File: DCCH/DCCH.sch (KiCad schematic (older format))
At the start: 37 parts, among them J1 Conn_01x02, J2 Conn_01x02, J3 Conn_01x05, J4 Conn_01x05, J5 Conn_02x08_Odd_Even, U11 SN74HC595, U12 SN74HC595, U13 SN74HC595, U14 SN74HC595, U21 SN754410, U22 SN754410, U23 SN754410, U24 SN754410

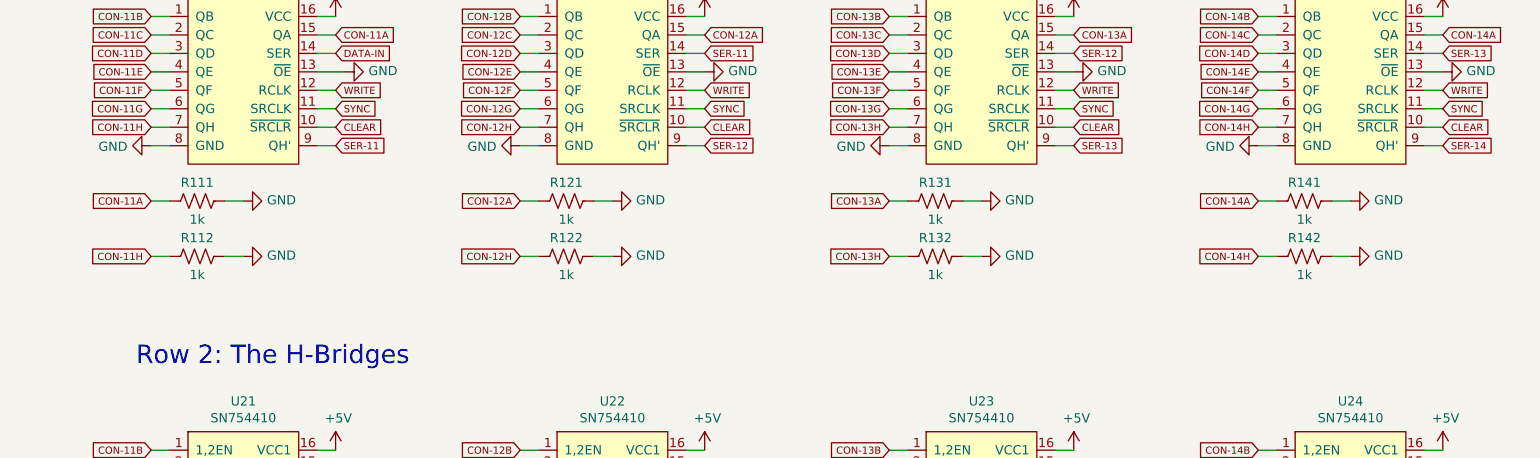
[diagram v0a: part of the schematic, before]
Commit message: Rewired everything. Removed the resistors. Now the control bit pattern for the shift registers makes sense.
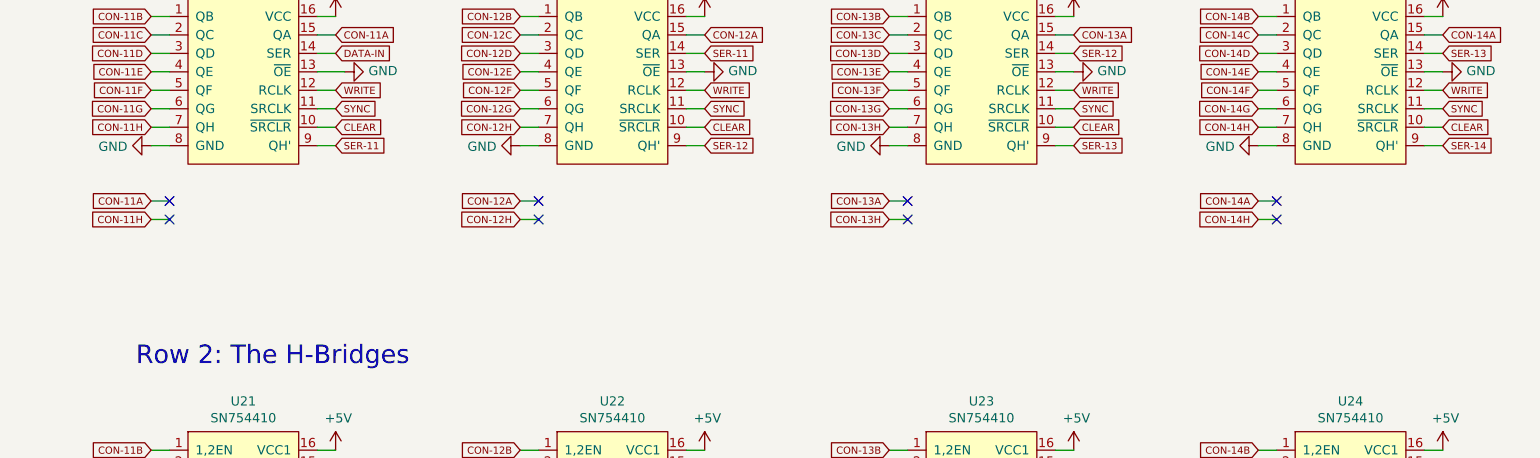
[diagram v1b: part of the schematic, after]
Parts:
- removed R111, R112, R121, R122, R131, R132, R141, R142: 1k, Resistor_THT:R_Axial_DIN0204_L3.6mm_D1.6mm_P5.08mm_Horizontal, symbol Device:R_US
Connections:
- no-connect marks 0 -> 8
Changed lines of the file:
@@
 Text GLabel 3300 2600 0    39   Input ~ 0
 CON-12A
-Text GLabel 3300 2900 0    39   Input ~ 0
+Text GLabel 3300 2700 0    39   Input ~ 0
 CON-12H
-$Comp
-L power:GND #PWR0151
-U 1 1 5F1FD99A
-P 3800 2600
-F 0 "#PWR0151" H 3800 2350 50  0001 C CNN
-F 1 "GND" V 3805 2472 50  0000 R CNN
-F 2 "" H 3800 2600 50  0001 C CNN
-F 3 "" H 3800 2600 50  0001 C CNN
-	1    3800 2600
-	0    -1   -1   0
-$EndComp
-Wire Wire Line
-	3700 2600 3800 2600
 Wire Wire Line
 	3300 2600 3400 2600
-$Comp
-L power:GND #PWR0150
-U 1 1 5F5CB761
-P 3800 2900
-F 0 "#PWR0150" H 3800 2650 50  0001 C CNN
-F 1 "GND" V 3805 2772 50  0000 R CNN
-F 2 "" H 3800 2900 50  0001 C CNN
-F 3 "" H 3800 2900 50  0001 C CNN
-	1    3800 2900
-	0    -1   -1   0
-$EndComp
-Wire Wire Line
-	3700 2900 3800 2900
-$Comp
-L Device:R_US R122
-U 1 1 5F5CB768
-P 3550 2900
-F 0 "R122" V 3450 2900 50  0000 C CNN
-F 1 "1k" V 3650 2900 50  0000 C CNN
-F 2 "Resistor_THT:R_Axial_DIN0204_L3.6mm_D1.6mm_P5.08mm_Horizontal" V 3590 2890 50  0001 C CNN
-F 3 "~" H 3550 2900 50  0001 C CNN
-	1    3550 2900
-	0    1    1    0
-$EndComp
-Wire Wire Line
-	3300 2900 3400 2900
+Wire Wire Line
+	3300 2700 3400 2700
 Text GLabel 1300 2600 0    39   Input ~ 0
 CON-11A
-Text GLabel 1300 2900 0    39   Input ~ 0
+Text GLabel 1300 2700 0    39   Input ~ 0
 CON-11H
-$Comp
-L power:GND #PWR0152
-U 1 1 5F6A8AEF
-P 1800 2600
-F 0 "#PWR0152" H 1800 2350 50  0001 C CNN
-F 1 "GND" V 1805 2472 50  0000 R CNN
-F 2 "" H 1800 2600 50  0001 C CNN
-F 3 "" H 1800 2600 50  0001 C CNN
-	1    1800 2600
-	0    -1   -1   0
-$EndComp
-Wire Wire Line
-	1700 2600 1800 2600
 Wire Wire Line
 	1300 2600 1400 2600
 Wire Wire Line
-	1300 2900 1400 2900
+	1300 2700 1400 2700
 Text GLabel 5300 2600 0    39   Input ~ 0
 CON-13A
-Text GLabel 5300 2900 0    39   Input ~ 0
+Text GLabel 5300 2700 0    39   Input ~ 0
 CON-13H
-$Comp
-L power:GND #PWR0154
-U 1 1 5F6BEDED
-P 5800 2600
-F 0 "#PWR0154" H 5800 2350 50  0001 C CNN
-F 1 "GND" V 5805 2472 50  0000 R CNN
-F 2 "" H 5800 2600 50  0001 C CNN
-F 3 "" H 5800 2600 50  0001 C CNN
-	1    5800 2600
-	0    -1   -1   0
-$EndComp
-Wire Wire Line
-	5700 2600 5800 2600
-$Comp
-L Device:R_US R131
-U 1 1 5F6BEDF4
-P 5550 2600
-F 0 "R131" V 5450 2600 50  0000 C CNN
-F 1 "1k" V 5650 2600 50  0000 C CNN
-F 2 "Resistor_THT:R_Axial_DIN0204_L3.6mm_D1.6mm_P5.08mm_Horizontal" V 5590 2590 50  0001 C CNN
-F 3 "~" H 5550 2600 50  0001 C CNN
-	1    5550 2600
-	0    1    1    0
-$EndComp
 Wire Wire Line
 	5300 2600 5400 2600
-$Comp
-L power:GND #PWR0155
-U 1 1 5F6BEDFB
-P 5800 2900
-F 0 "#PWR0155" H 5800 2650 50  0001 C CNN
-F 1 "GND" V 5805 2772 50  0000 R CNN
-F 2 "" H 5800 2900 50  0001 C CNN
-F 3 "" H 5800 2900 50  0001 C CNN
-	1    5800 2900
-	0    -1   -1   0
-$EndComp
-Wire Wire Line
-	5700 2900 5800 2900
-$Comp
-L Device:R_US R132
-U 1 1 5F6BEE02
-P 5550 2900
-F 0 "R132" V 5450 2900 50  0000 C CNN
-F 1 "1k" V 5650 2900 50  0000 C CNN
-F 2 "Resistor_THT:R_Axial_DIN0204_L3.6mm_D1.6mm_P5.08mm_Horizontal" V 5590 2890 50  0001 C CNN
-F 3 "~" H 5550 2900 50  0001 C CNN
-	1    5550 2900
-	0    1    1    0
-$EndComp
-Wire Wire Line
-	5300 2900 5400 2900
+Wire Wire Line
+	5300 2700 5400 2700
 Text GLabel 7300 2600 0    39   Input ~ 0
 CON-14A
-Text GLabel 7300 2900 0    39   Input ~ 0
+Text GLabel 7300 2700 0    39   Input ~ 0
 CON-14H
-$Comp
-L power:GND #PWR0156
-U 1 1 5F6EC70B
-P 7800 2600
-F 0 "#PWR0156" H 7800 2350 50  0001 C CNN
-F 1 "GND" V 7805 2472 50  0000 R CNN
-F 2 "" H 7800 2600 50  0001 C CNN
-F 3 "" H 7800 2600 50  0001 C CNN
-	1    7800 2600
-	0    -1   -1   0
-$EndComp
-Wire Wire Line
-	7700 2600 7800 2600
-$Comp
-L Device:R_US R141
-U 1 1 5F6EC712
-P 7550 2600
-F 0 "R141" V 7450 2600 50  0000 C CNN
-F 1 "1k" V 7650 2600 50  0000 C CNN
-F 2 "Resistor_THT:R_Axial_DIN0204_L3.6mm_D1.6mm_P5.08mm_Horizontal" V 7590 2590 50  0001 C CNN
-F 3 "~" H 7550 2600 50  0001 C CNN
-	1    7550 2600
-	0    1    1    0
-$EndComp
 Wire Wire Line
 	7300 2600 7400 2600
-$Comp
-L power:GND #PWR0157
-U 1 1 5F6EC719
-P 7800 2900
-F 0 "#PWR0157" H 7800 2650 50  0001 C CNN
-F 1 "GND" V 7805 2772 50  0000 R CNN
-F 2 "" H 7800 2900 50  0001 C CNN
-F 3 "" H 7800 2900 50  0001 C CNN
-	1    7800 2900
-	0    -1   -1   0
-$EndComp
-Wire Wire Line
-	7700 2900 7800 2900
-$Comp
-L Device:R_US R142
-U 1 1 5F6EC720
-P 7550 2900
-F 0 "R142" V 7450 2900 50  0000 C CNN
-F 1 "1k" V 7650 2900 50  0000 C CNN
-F 2 "Resistor_THT:R_Axial_DIN0204_L3.6mm_D1.6mm_P5.08mm_Horizontal" V 7590 2890 50  0001 C CNN
-F 3 "~" H 7550 2900 50  0001 C CNN
-	1    7550 2900
-	0    1    1    0
-$EndComp
-Wire Wire Line
-	7300 2900 7400 2900
-$Comp
-L Device:R_US R121
-U 1 1 5F270496
-P 3550 2600
-F 0 "R121" V 3450 2600 50  0000 C CNN
-F 1 "1k" V 3650 2600 50  0000 C CNN
-F 2 "Resistor_THT:R_Axial_DIN0204_L3.6mm_D1.6mm_P5.08mm_Horizontal" V 3590 2590 50  0001 C CNN
-F 3 "~" H 3550 2600 50  0001 C CNN
-	1    3550 2600
-	0    1    1    0
-$EndComp
-$Comp
-L Device:R_US R111
-U 1 1 5F6A8AF6
-P 1550 2600
-F 0 "R111" V 1450 2600 50  0000 C CNN
-F 1 "1k" V 1650 2600 50  0000 C CNN
-F 2 "Resistor_THT:R_Axial_DIN0204_L3.6mm_D1.6mm_P5.08mm_Horizontal" V 1590 2590 50  0001 C CNN
-F 3 "~" H 1550 2600 50  0001 C CNN
-	1    1550 2600
-	0    1    1    0
-$EndComp
-$Comp
-L Device:R_US R112
-U 1 1 5F6A8B04
-P 1550 2900
-F 0 "R112" V 1450 2900 50  0000 C CNN
-F 1 "1k" V 1650 2900 50  0000 C CNN
-F 2 "Resistor_THT:R_Axial_DIN0204_L3.6mm_D1.6mm_P5.08mm_Horizontal" V 1590 2890 50  0001 C CNN
-F 3 "~" H 1550 2900 50  0001 C CNN
-	1    1550 2900
-	0    1    1    0
-$EndComp
-Wire Wire Line
-	1700 2900 1800 2900
-$Comp
-L power:GND #PWR0153
-U 1 1 5F6A8AFD
-P 1800 2900
-F 0 "#PWR0153" H 1800 2650 50  0001 C CNN
-F 1 "GND" V 1805 2772 50  0000 R CNN
-F 2 "" H 1800 2900 50  0001 C CNN
-F 3 "" H 1800 2900 50  0001 C CNN
-	1    1800 2900
-	0    -1   -1   0
-$EndComp
+Wire Wire Line
+	7300 2700 7400 2700
 Text Notes 2700 3500 2    100  ~ 0
 Row 2: The H-Bridges
@@
 Text GLabel 8300 4050 2    39   Input ~ 0
 CON-14G
+NoConn ~ 1400 2600
+NoConn ~ 1400 2700
+NoConn ~ 3400 2600
+NoConn ~ 3400 2700
+NoConn ~ 5400 2600
+NoConn ~ 5400 2700
+NoConn ~ 7400 2600
+NoConn ~ 7400 2700
 $EndSCHEMATC

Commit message: Fixed WRITE and SYNC pins, as they were mixed up.
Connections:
- net SYNC: now also J3.2 (Pin_2), J4.2 (Pin_2), U11.12 (RCLK), U12.12 (RCLK), U13.12 (RCLK), U14.12 (RCLK); no longer J3.3 (Pin_3), J4.3 (Pin_3), U11.11 (SRCLK), U12.11 (SRCLK), U13.11 (SRCLK), U14.11 (SRCLK)
- net WRITE: now also J3.3 (Pin_3), J4.3 (Pin_3), U11.11 (SRCLK), U12.11 (SRCLK), U13.11 (SRCLK), U14.11 (SRCLK); no longer J3.2 (Pin_2), J4.2 (Pin_2), U11.12 (RCLK), U12.12 (RCLK), U13.12 (RCLK), U14.12 (RCLK)
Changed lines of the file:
@@
 Text GLabel 10050 2850 0    39   Input ~ 0
 CLEAR
+Text GLabel 10050 2650 0    39   Input ~ 0
+SYNC
 Text GLabel 10050 2750 0    39   Input ~ 0
-SYNC
-Text GLabel 10050 2650 0    39   Input ~ 0
 WRITE
 Text GLabel 10050 2550 0    39   Input ~ 0
@@
 Text GLabel 10050 3850 0    39   Input ~ 0
 CLEAR
+Text GLabel 10050 3650 0    39   Input ~ 0
+SYNC
 Text GLabel 10050 3750 0    39   Input ~ 0
-SYNC
-Text GLabel 10050 3650 0    39   Input ~ 0
 WRITE
 $Comp
@@
 Wire Wire Line
 	6200 2000 6300 2000
+Text GLabel 6300 2100 2    39   Input ~ 0
+WRITE
 Text GLabel 6300 2000 2    39   Input ~ 0
-WRITE
-Text GLabel 6300 2100 2    39   Input ~ 0
 SYNC
 Text GLabel 6300 2200 2    39   Input ~ 0
@@
 Wire Wire Line
 	4200 2000 4300 2000
+Text GLabel 4300 2100 2    39   Input ~ 0
+WRITE
 Text GLabel 4300 2000 2    39   Input ~ 0
-WRITE
-Text GLabel 4300 2100 2    39   Input ~ 0
 SYNC
 Text GLabel 4300 2200 2    39   Input ~ 0
@@
 Text GLabel 2300 1800 2    39   Input ~ 0
 DATA-IN
+Text GLabel 2300 2100 2    39   Input ~ 0
+WRITE
 Text GLabel 2300 2000 2    39   Input ~ 0
-WRITE
-Text GLabel 2300 2100 2    39   Input ~ 0
 SYNC
 Text GLabel 2300 2200 2    39   Input ~ 0
@@
 Wire Wire Line
 	8200 2000 8300 2000
+Text GLabel 8300 2100 2    39   Input ~ 0
+WRITE
 Text GLabel 8300 2000 2    39   Input ~ 0
-WRITE
-Text GLabel 8300 2100 2    39   Input ~ 0
 SYNC
 Text GLabel 8300 2200 2    39   Input ~ 0

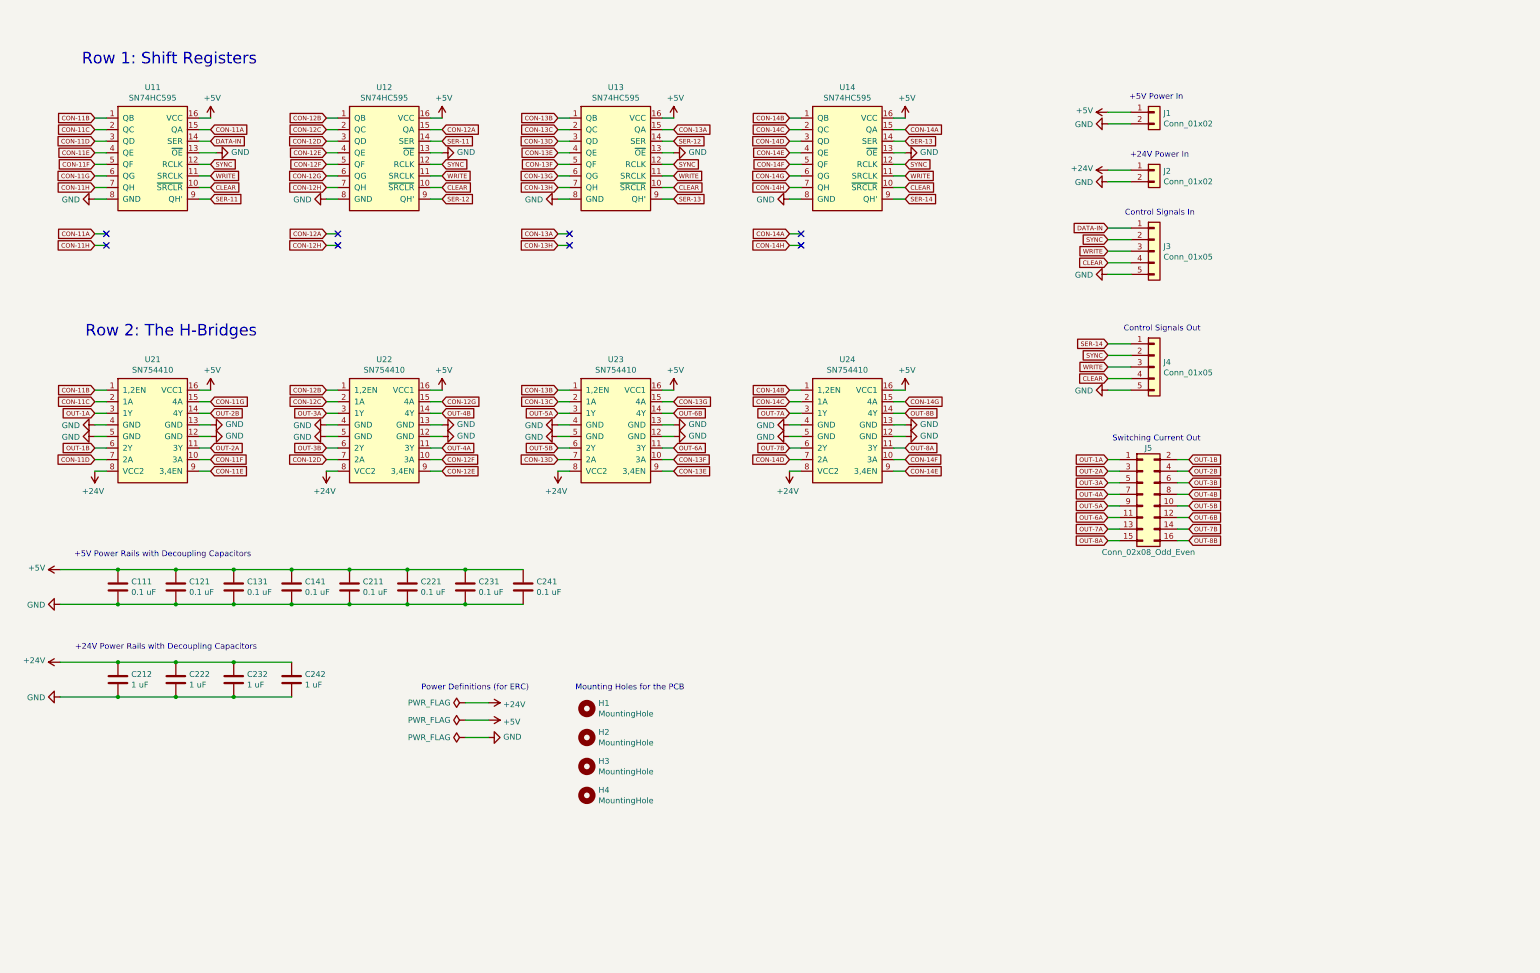
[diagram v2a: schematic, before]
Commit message: Changed board layout once again. Updated schematic. Updated board.
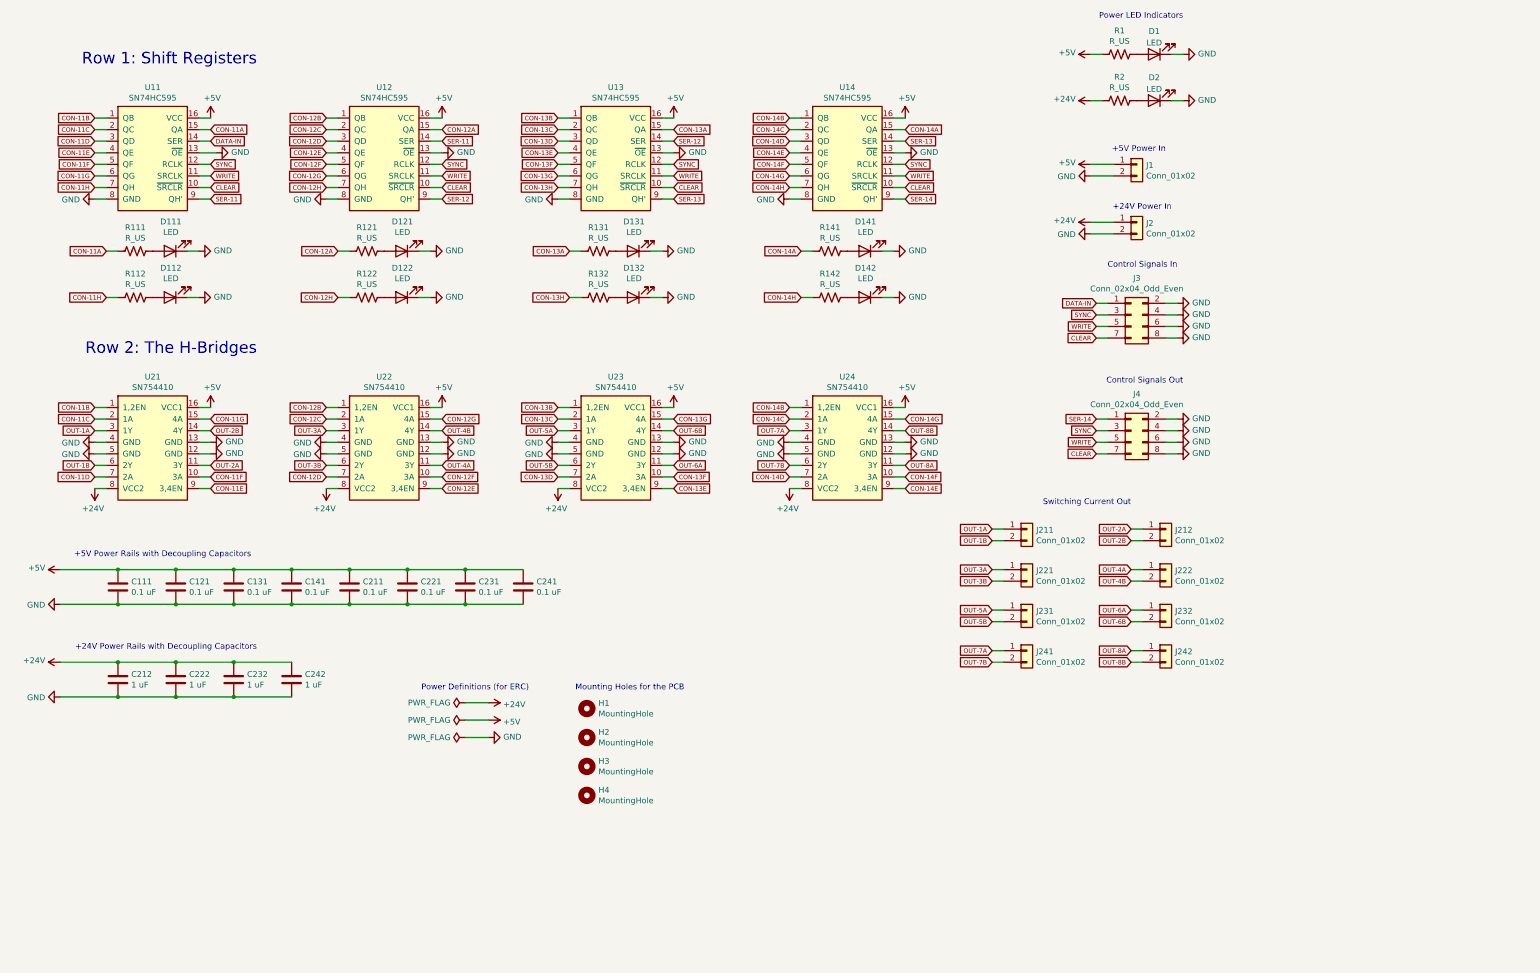
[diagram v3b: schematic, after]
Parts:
- removed J3, J4: Conn_01x05, Connector_PinHeader_2.54mm:PinHeader_1x05_P2.54mm_Vertical, symbol Connector_Generic:Conn_01x05
- removed J5: Conn_02x08_Odd_Even, Connector_PinHeader_2.54mm:PinHeader_2x08_P2.54mm_Vertical, symbol Connector_Generic:Conn_02x08_Odd_Even
- added D1, D111, D112, D121, D122, D131, D132, D141, D142, D2: LED, LED_SMD:LED_0805_2012Metric, symbol Device:LED
- added J211, J212, J221, J222, J231, J232, J241, J242: Conn_01x02, Connector_PinHeader_2.54mm:PinHeader_1x02_P2.54mm_Vertical, symbol Connector_Generic:Conn_01x02
- added J3, J4: Conn_02x04_Odd_Even, Connector_PinHeader_2.54mm:PinHeader_2x04_P2.54mm_Vertical, symbol Connector_Generic:Conn_02x04_Odd_Even
- added R1, R111, R112, R121, R122, R131, R132, R141, R142, R2: R_US, Resistor_SMD:R_0805_2012Metric, symbol Device:R_US
- J1, J2: footprint Connector_PinHeader_2.54mm:PinHeader_1x02_P2.54mm_Vertical -> Connector_Phoenix_MC:PhoenixContact_MC_1,5_2-GF-3.5_1x02_P3.50mm_Horizontal_ThreadedFlange_MountHole
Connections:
- net +24V: now also R2.2
- net +5V: now also R1.2
- net CLEAR: now also J3.7 (Pin_7), J4.7 (Pin_7)
- net CON-11A: now also R111.2
- net CON-11H: now also R112.2
- net CON-12A: now also R121.2
- net CON-12H: now also R122.2
- net CON-13A: now also R131.2
- net CON-13H: now also R132.2
- net CON-14A: now also R141.2
- net CON-14H: now also R142.2
- net DATA-IN: now also J3.1 (Pin_1)
- net GND: now also D1.1 (K), D111.1 (K), D112.1 (K), D121.1 (K), D122.1 (K), D131.1 (K), D132.1 (K), D141.1 (K), D142.1 (K), D2.1 (K), J3.2 (Pin_2), J3.4 (Pin_4), J3.6 (Pin_6), J3.8 (Pin_8), J4.2 (Pin_2), J4.4 (Pin_4), J4.6 (Pin_6), J4.8 (Pin_8)
- net OUT-1A: now also J211.1 (Pin_1)
- net OUT-1B: now also J211.2 (Pin_2)
- net OUT-2A: now also J212.1 (Pin_1)
- net OUT-2B: now also J212.2 (Pin_2)
- net OUT-3A: now also J221.1 (Pin_1)
- net OUT-3B: now also J221.2 (Pin_2)
- net OUT-4A: now also J222.1 (Pin_1)
- net OUT-4B: now also J222.2 (Pin_2)
- net OUT-5A: now also J231.1 (Pin_1)
- net OUT-5B: now also J231.2 (Pin_2)
- net OUT-6A: now also J232.1 (Pin_1)
- net OUT-6B: now also J232.2 (Pin_2)
- net OUT-7A: now also J241.1 (Pin_1)
- net OUT-7B: now also J241.2 (Pin_2)
- net OUT-8A: now also J242.1 (Pin_1)
- net OUT-8B: now also J242.2 (Pin_2)
- net SER-14: now also J4.1 (Pin_1)
- net SYNC: now also J3.3 (Pin_3), J4.3 (Pin_3)
- net WRITE: now also J3.5 (Pin_5), J4.5 (Pin_5)
- new net: D111.2 (A), R111.1
- new net: D112.2 (A), R112.1
- new net: D121.2 (A), R121.1
- new net: D122.2 (A), R122.1
- new net: D131.2 (A), R131.1
- new net: D132.2 (A), R132.1
- new net: D141.2 (A), R141.1
- new net: D142.2 (A), R142.1
- new net: D1.2 (A), R1.1
- new net: D2.2 (A), R2.1
- no-connect marks 8 -> 0
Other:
- note added: "Power LED Indicators"
- moved on the sheet: J1, J2, U21, U22, U23, U24

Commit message: Changed orientation again.
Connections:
- net CLEAR: now also J4.8 (Pin_8); no longer J4.7 (Pin_7)
- net GND: now also J4.1 (Pin_1), J4.3 (Pin_3), J4.5 (Pin_5), J4.7 (Pin_7); no longer J4.2 (Pin_2), J4.4 (Pin_4), J4.6 (Pin_6), J4.8 (Pin_8)
- net SER-14: now also J4.2 (Pin_2); no longer J4.1 (Pin_1)
- net SYNC: now also J4.4 (Pin_4); no longer J4.3 (Pin_3)
- net WRITE: now also J4.6 (Pin_6); no longer J4.5 (Pin_5)
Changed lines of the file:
@@
 L Connector_Generic:Conn_02x04_Odd_Even J4
 U 1 1 5F16B572
-P 10250 4300
-F 0 "J4" H 10300 4617 50  0000 C CNN
-F 1 "Conn_02x04_Odd_Even" H 10300 4526 50  0000 C CNN
-F 2 "Connector_PinHeader_2.54mm:PinHeader_2x04_P2.54mm_Vertical" H 10250 4300 50  0001 C CNN
-F 3 "~" H 10250 4300 50  0001 C CNN
-	1    10250 4300
-	1    0    0    -1
+P 10350 4300
+F 0 "J4" H 10400 4617 50  0000 C CNN
+F 1 "Conn_02x04_Odd_Even" H 10400 4526 50  0000 C CNN
+F 2 "Connector_PinHeader_2.54mm:PinHeader_2x04_P2.54mm_Vertical" H 10350 4300 50  0001 C CNN
+F 3 "~" H 10350 4300 50  0001 C CNN
+	1    10350 4300
+	-1   0    0    -1
 $EndComp
 $EndSCHEMATC
